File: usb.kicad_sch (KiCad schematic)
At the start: 17 parts, among them J2 USB_C_Receptacle, J3 Conn_01x02_Pin, Q1 STL6N3LLH6, U5 TCPP01-M12, U6 USBLC6-2P6, U7 STEF05SGR

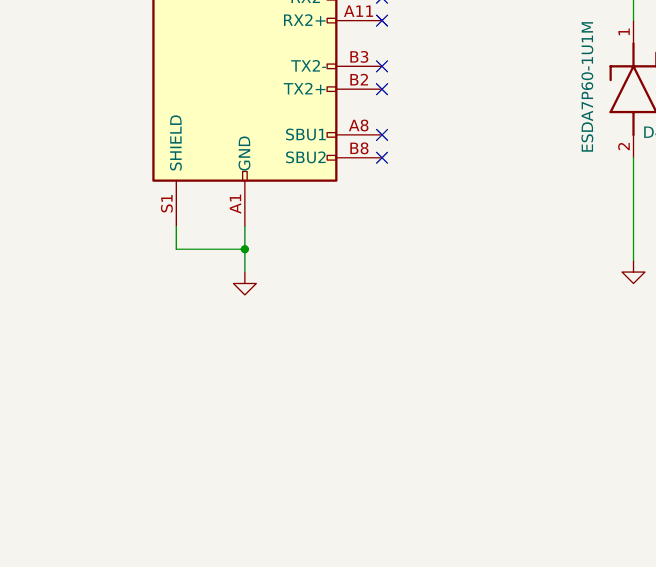
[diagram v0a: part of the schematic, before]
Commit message: only usb powered
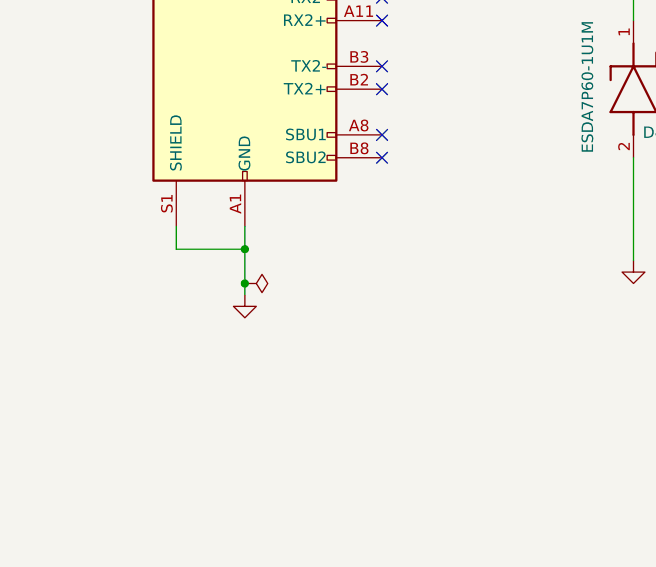
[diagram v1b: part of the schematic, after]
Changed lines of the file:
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@@
 	)
 	(junction
+		(at 33.02 132.08)
+		(diameter 0)
+		(color 0 0 0 0)
+	)
+	(junction
 		(at 267.97 110.49)
 		(diameter 0)
@@
 	(wire
 		(pts
+			(xy 33.02 132.08) (xy 33.02 133.35)
+		)
+		(stroke
+			(width 0)
+			(type default)
+		)
+	)
+	(wire
+		(pts
 			(xy 247.65 113.03) (xy 267.97 113.03)
 		)
@@
 	(wire
 		(pts
-			(xy 33.02 128.27) (xy 33.02 130.81)
+			(xy 33.02 128.27) (xy 33.02 132.08)
 		)
 		(stroke
@@
 			(project ""
 				(path "/e660428c-c9b7-476c-8ac8-2d419f233469/7dd15615-8075-471d-b8bf-599b8660331d"
-					(reference "R401")
+					(reference "R201")
 					(unit 1)
 				)
@@
 			(project ""
 				(path "/e660428c-c9b7-476c-8ac8-2d419f233469/7dd15615-8075-471d-b8bf-599b8660331d"
-					(reference "#PWR0409")
+					(reference "#PWR0209")
 					(unit 1)
 				)
@@
 	(symbol
 		(lib_id "power:GND")
-		(at 33.02 130.81 0)
+		(at 33.02 133.35 0)
 		(unit 1)
 		(exclude_from_sim no)
@@
 		(fields_autoplaced yes)
 		(property "Reference" "#PWR041"
-			(at 33.02 137.16 0)
+			(at 33.02 139.7 0)
 			(effects
 				(font
@@
 		)
 		(property "Value" "GND"
-			(at 33.02 135.89 0)
+			(at 33.02 138.43 0)
 			(effects
 				(font
@@
 		)
 		(property "Footprint" ""
-			(at 33.02 130.81 0)
+			(at 33.02 133.35 0)
 			(effects
 				(font
@@
 		)
 		(property "Datasheet" ""
-			(at 33.02 130.81 0)
+			(at 33.02 133.35 0)
 			(effects
 				(font
@@
 		)
 		(property "Description" "Power symbol creates a global label with name \"GND\" , ground"
-			(at 33.02 130.81 0)
+			(at 33.02 133.35 0)
 			(effects
 				(font
@@
 			(project ""
 				(path "/e660428c-c9b7-476c-8ac8-2d419f233469/7dd15615-8075-471d-b8bf-599b8660331d"
-					(reference "#PWR0413")
+					(reference "#PWR0214")
 					(unit 1)
 				)
@@
 			(project ""
 				(path "/e660428c-c9b7-476c-8ac8-2d419f233469/7dd15615-8075-471d-b8bf-599b8660331d"
-					(reference "#PWR0412")
+					(reference "#PWR0212")
 					(unit 1)
 				)
@@
 			(project ""
 				(path "/e660428c-c9b7-476c-8ac8-2d419f233469/7dd15615-8075-471d-b8bf-599b8660331d"
-					(reference "#PWR0411")
+					(reference "#PWR0211")
 					(unit 1)
 				)
@@
 			(project ""
 				(path "/e660428c-c9b7-476c-8ac8-2d419f233469/7dd15615-8075-471d-b8bf-599b8660331d"
-					(reference "#PWR0407")
+					(reference "#PWR0207")
 					(unit 1)
 				)
@@
 			(project ""
 				(path "/e660428c-c9b7-476c-8ac8-2d419f233469/7dd15615-8075-471d-b8bf-599b8660331d"
-					(reference "D402")
+					(reference "D202")
 					(unit 1)
 				)
@@
 			(project ""
 				(path "/e660428c-c9b7-476c-8ac8-2d419f233469/7dd15615-8075-471d-b8bf-599b8660331d"
-					(reference "#PWR0419")
+					(reference "#PWR0219")
 					(unit 1)
 				)
@@
 			(project ""
 				(path "/e660428c-c9b7-476c-8ac8-2d419f233469/7dd15615-8075-471d-b8bf-599b8660331d"
-					(reference "D401")
+					(reference "D201")
 					(unit 1)
 				)
@@
 			(project ""
 				(path "/e660428c-c9b7-476c-8ac8-2d419f233469/7dd15615-8075-471d-b8bf-599b8660331d"
-					(reference "#PWR0408")
+					(reference "#PWR0208")
 					(unit 1)
 				)
@@
 			(project ""
 				(path "/e660428c-c9b7-476c-8ac8-2d419f233469/7dd15615-8075-471d-b8bf-599b8660331d"
-					(reference "#PWR0418")
+					(reference "#PWR0218")
 					(unit 1)
 				)
@@
 			(project ""
 				(path "/e660428c-c9b7-476c-8ac8-2d419f233469/7dd15615-8075-471d-b8bf-599b8660331d"
-					(reference "#FLG0403")
+					(reference "#FLG0203")
 					(unit 1)
 				)
@@
 			(project ""
 				(path "/e660428c-c9b7-476c-8ac8-2d419f233469/7dd15615-8075-471d-b8bf-599b8660331d"
-					(reference "#PWR0406")
+					(reference "#PWR0206")
 					(unit 1)
 				)
@@
 			(project ""
 				(path "/e660428c-c9b7-476c-8ac8-2d419f233469/7dd15615-8075-471d-b8bf-599b8660331d"
-					(reference "#PWR0410")
+					(reference "#PWR0210")
 					(unit 1)
 				)
@@
 			(project ""
 				(path "/e660428c-c9b7-476c-8ac8-2d419f233469/7dd15615-8075-471d-b8bf-599b8660331d"
-					(reference "#PWR0401")
+					(reference "#PWR0201")
 					(unit 1)
 				)
@@
 			(project ""
 				(path "/e660428c-c9b7-476c-8ac8-2d419f233469/7dd15615-8075-471d-b8bf-599b8660331d"
-					(reference "J402")
+					(reference "J202")
 					(unit 1)
 				)
@@
 			(project ""
 				(path "/e660428c-c9b7-476c-8ac8-2d419f233469/7dd15615-8075-471d-b8bf-599b8660331d"
-					(reference "Q401")
+					(reference "Q201")
 					(unit 1)
 				)
@@
 			(project ""
 				(path "/e660428c-c9b7-476c-8ac8-2d419f233469/7dd15615-8075-471d-b8bf-599b8660331d"
-					(reference "U401")
+					(reference "U201")
 					(unit 1)
 				)
@@
 			(project ""
 				(path "/e660428c-c9b7-476c-8ac8-2d419f233469/7dd15615-8075-471d-b8bf-599b8660331d"
-					(reference "#FLG0402")
+					(reference "#FLG0202")
 					(unit 1)
 				)
@@
 			(project ""
 				(path "/e660428c-c9b7-476c-8ac8-2d419f233469/7dd15615-8075-471d-b8bf-599b8660331d"
-					(reference "TP402")
+					(reference "TP202")
+					(unit 1)
+				)
+			)
+		)
+	)
+	(symbol
+		(lib_id "power:PWR_FLAG")
+		(at 33.02 132.08 270)
+		(unit 1)
+		(exclude_from_sim no)
+		(in_bom yes)
+		(on_board yes)
+		(dnp no)
+		(fields_autoplaced yes)
+		(property "Reference" "#FLG0204"
+			(at 34.925 132.08 0)
+			(effects
+				(font
+					(size 1.27 1.27)
+				)
+				(hide yes)
+			)
+		)
+		(property "Value" "PWR_FLAG"
+			(at 36.83 132.0801 90)
+			(effects
+				(font
+					(size 1.27 1.27)
+				)
+				(justify left)
+				(hide yes)
+			)
+		)
+		(property "Footprint" ""
+			(at 33.02 132.08 0)
+			(effects
+				(font
+					(size 1.27 1.27)
+				)
+				(hide yes)
+			)
+		)
+		(property "Datasheet" "~"
+			(at 33.02 132.08 0)
+			(effects
+				(font
+					(size 1.27 1.27)
+				)
+				(hide yes)
+			)
+		)
+		(property "Description" "Special symbol for telling ERC where power comes from"
+			(at 33.02 132.08 0)
+			(effects
+				(font
+					(size 1.27 1.27)
+				)
+				(hide yes)
+			)
+		)
+		(pin "1"
+		)
+		(instances
+			(project "EnergyMonitoringSystem"
+				(path "/e660428c-c9b7-476c-8ac8-2d419f233469/7dd15615-8075-471d-b8bf-599b8660331d"
+					(reference "#FLG0204")
 					(unit 1)
 				)
@@
 			(project ""
 				(path "/e660428c-c9b7-476c-8ac8-2d419f233469/7dd15615-8075-471d-b8bf-599b8660331d"
-					(reference "J401")
+					(reference "J201")
 					(unit 1)
 				)
@@
 			(project ""
 				(path "/e660428c-c9b7-476c-8ac8-2d419f233469/7dd15615-8075-471d-b8bf-599b8660331d"
-					(reference "#PWR0416")
+					(reference "#PWR0216")
 					(unit 1)
 				)
@@
 			(project ""
 				(path "/e660428c-c9b7-476c-8ac8-2d419f233469/7dd15615-8075-471d-b8bf-599b8660331d"
-					(reference "R402")
+					(reference "R202")
 					(unit 1)
 				)
@@
 			(project ""
 				(path "/e660428c-c9b7-476c-8ac8-2d419f233469/7dd15615-8075-471d-b8bf-599b8660331d"
-					(reference "C404")
+					(reference "C204")
 					(unit 1)
 				)
@@
 			(project ""
 				(path "/e660428c-c9b7-476c-8ac8-2d419f233469/7dd15615-8075-471d-b8bf-599b8660331d"
-					(reference "TP401")
+					(reference "TP201")
 					(unit 1)
 				)
@@
 			(project ""
 				(path "/e660428c-c9b7-476c-8ac8-2d419f233469/7dd15615-8075-471d-b8bf-599b8660331d"
-					(reference "U402")
+					(reference "U202")
 					(unit 1)
 				)
@@
 			(project ""
 				(path "/e660428c-c9b7-476c-8ac8-2d419f233469/7dd15615-8075-471d-b8bf-599b8660331d"
-					(reference "#PWR0404")
+					(reference "#PWR0204")
 					(unit 1)
 				)
@@
 			(project ""
 				(path "/e660428c-c9b7-476c-8ac8-2d419f233469/7dd15615-8075-471d-b8bf-599b8660331d"
-					(reference "U403")
+					(reference "U203")
 					(unit 1)
 				)
@@
 			(project ""
 				(path "/e660428c-c9b7-476c-8ac8-2d419f233469/7dd15615-8075-471d-b8bf-599b8660331d"
-					(reference "#PWR0417")
+					(reference "#PWR0217")
 					(unit 1)
 				)
@@
 			(project ""
 				(path "/e660428c-c9b7-476c-8ac8-2d419f233469/7dd15615-8075-471d-b8bf-599b8660331d"
-					(reference "#PWR0402")
+					(reference "#PWR0202")
 					(unit 1)
 				)
@@
 			(project ""
 				(path "/e660428c-c9b7-476c-8ac8-2d419f233469/7dd15615-8075-471d-b8bf-599b8660331d"
-					(reference "#PWR0405")
+					(reference "#PWR0205")
 					(unit 1)
 				)
@@
 			(project ""
 				(path "/e660428c-c9b7-476c-8ac8-2d419f233469/7dd15615-8075-471d-b8bf-599b8660331d"
-					(reference "#PWR0415")
+					(reference "#PWR0215")
 					(unit 1)
 				)
@@
 			(project ""
 				(path "/e660428c-c9b7-476c-8ac8-2d419f233469/7dd15615-8075-471d-b8bf-599b8660331d"
-					(reference "R403")
+					(reference "R203")
 					(unit 1)
 				)
@@
 			(project ""
 				(path "/e660428c-c9b7-476c-8ac8-2d419f233469/7dd15615-8075-471d-b8bf-599b8660331d"
-					(reference "C401")
+					(reference "C201")
 					(unit 1)
 				)
@@
 			(project ""
 				(path "/e660428c-c9b7-476c-8ac8-2d419f233469/7dd15615-8075-471d-b8bf-599b8660331d"
-					(reference "C403")
+					(reference "C203")
 					(unit 1)
 				)
@@
 			(project ""
 				(path "/e660428c-c9b7-476c-8ac8-2d419f233469/7dd15615-8075-471d-b8bf-599b8660331d"
-					(reference "#PWR0403")
+					(reference "#PWR0203")
 					(unit 1)
 				)
@@
 			(project ""
 				(path "/e660428c-c9b7-476c-8ac8-2d419f233469/7dd15615-8075-471d-b8bf-599b8660331d"
-					(reference "C402")
+					(reference "C202")
 					(unit 1)
 				)
@@
 			(project ""
 				(path "/e660428c-c9b7-476c-8ac8-2d419f233469/7dd15615-8075-471d-b8bf-599b8660331d"
-					(reference "#PWR0414")
+					(reference "#PWR0213")
 					(unit 1)
 				)
@@
 			(project ""
 				(path "/e660428c-c9b7-476c-8ac8-2d419f233469/7dd15615-8075-471d-b8bf-599b8660331d"
-					(reference "#FLG0401")
+					(reference "#FLG0201")
 					(unit 1)
 				)

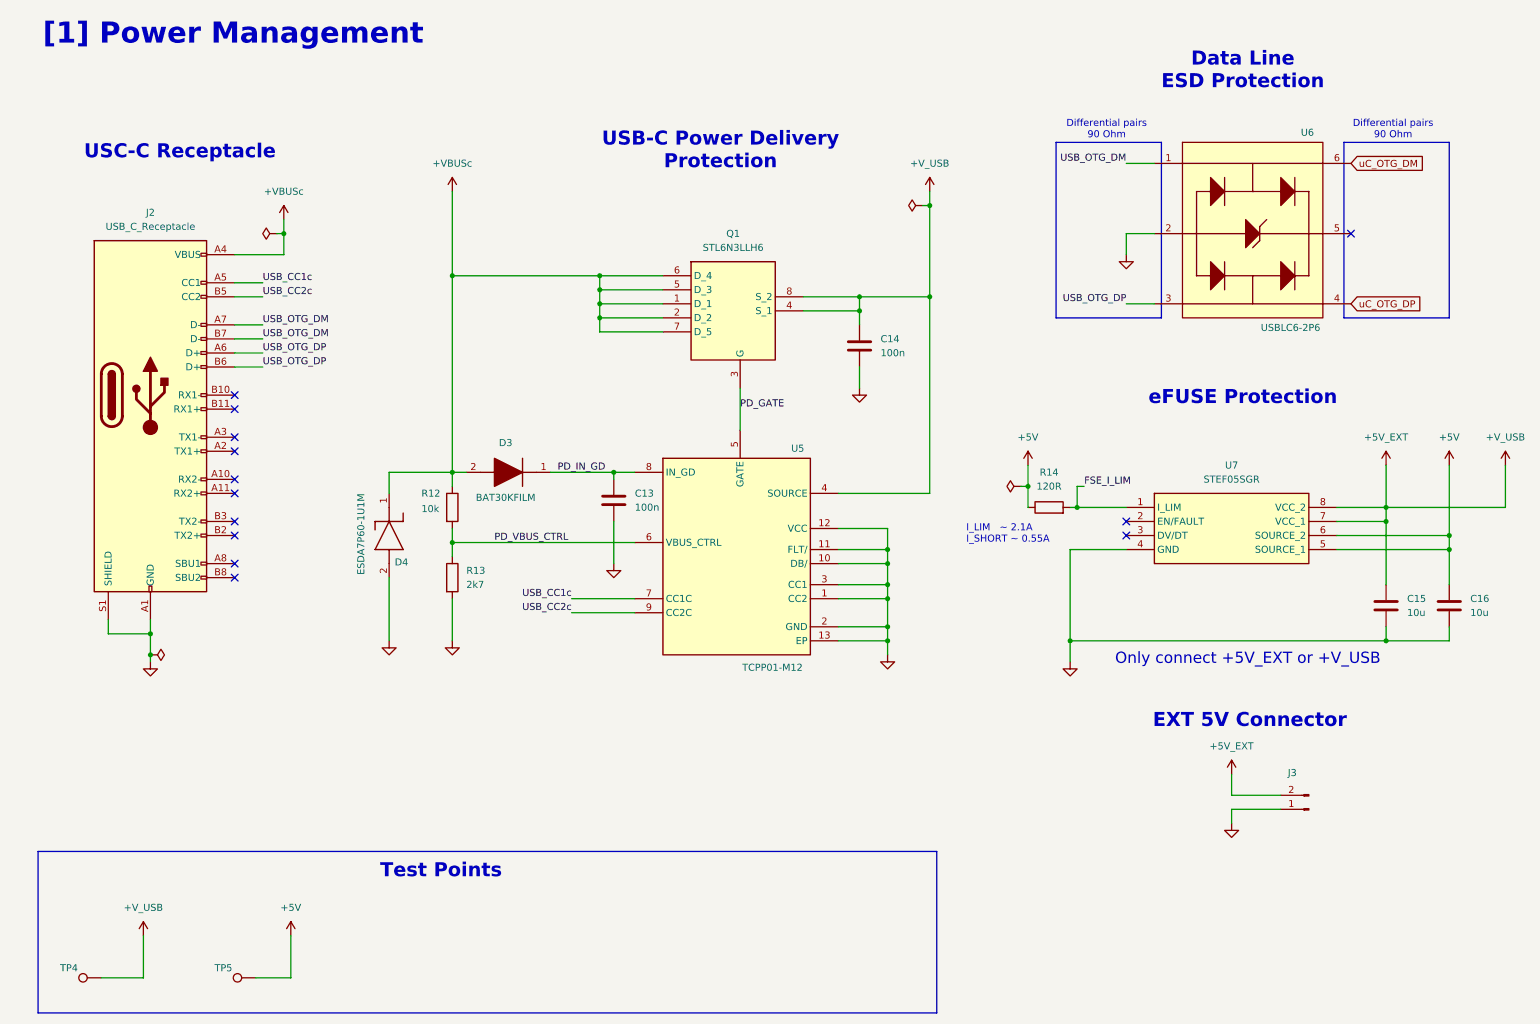
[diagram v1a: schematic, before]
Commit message: components with distributor links added
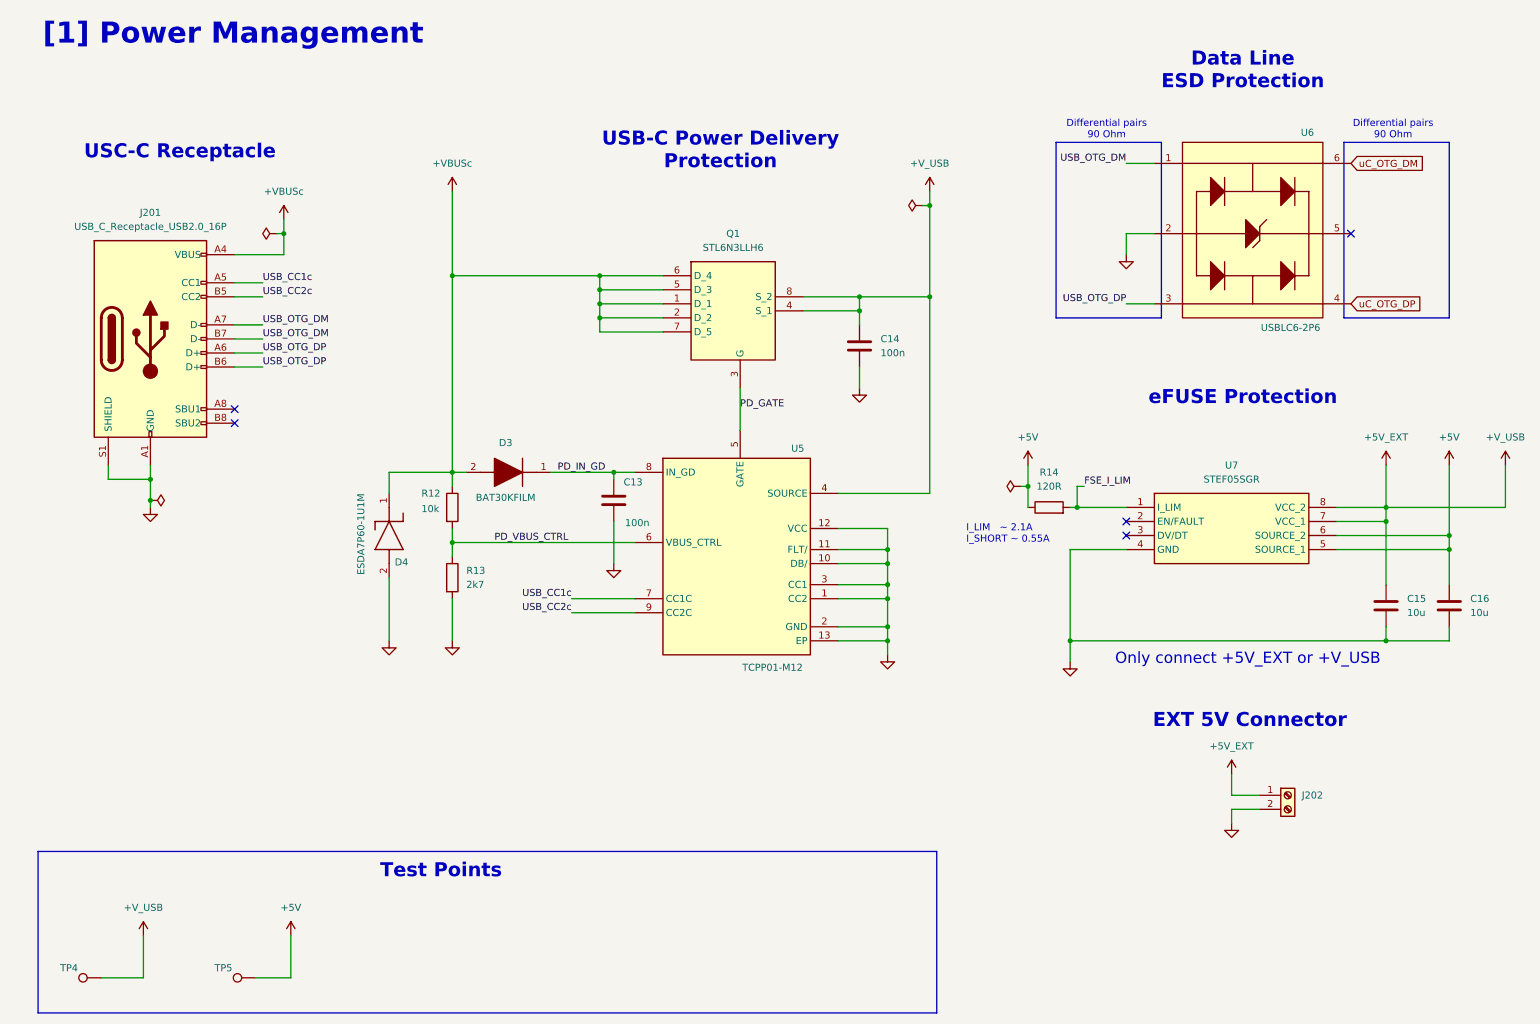
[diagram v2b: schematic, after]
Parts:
- removed J2: USB_C_Receptacle, Connector_USB:USB_C_Receptacle_GCT_USB4105-xx-A_16P_TopMnt_Horizontal, symbol Connector:USB_C_Receptacle
- removed J3: Conn_01x02_Pin, TerminalBlock_Phoenix:TerminalBlock_Phoenix_MKDS-1,5-2-5.08_1x02_P5.08mm_Horizontal, symbol Connector:Conn_01x02_Pin
- added J201: USB_C_Receptacle_USB2.0_16P, Connector_USB:USB_C_Receptacle_GCT_USB4105-xx-A_16P_TopMnt_Horizontal, symbol Connector:USB_C_Receptacle_USB2.0_16P
- added J202: Screw_Terminal_01x02, TerminalBlock_Phoenix:TerminalBlock_Phoenix_MKDS-1,5-2-5.08_1x02_P5.08mm_Horizontal, symbol Connector:Screw_Terminal_01x02
- C13, C14: Distributor_Link (none) -> https://www.mouser.com/ProductDetail/KYOCERA-AVX/04023C104K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; Manufacturer_Name (none) -> KYOCERA AVX; Manufacturer_Part_Number (none) -> 04023C104KAT2A
- C15, C16: Distributor_Link (none) -> https://www.mouser.com/ProductDetail/KYOCERA-AVX/KGM15CR51A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; Manufacturer_Name (none) -> KYOCERA AVX; Manufacturer_Part_Number (none) -> KGM15CR51A106KT
- D3: Distributor_Link (none) -> https://www.mouser.co.uk/ProductDetail/STMicroelectronics/B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
- D4: Distributor_Link (none) -> https://www.mouser.co.uk/ProductDetail/STMicroelectronics/E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
- Q1, U7: Distributor_Link (none) -> https://www.mouser.co.uk/ProductDetail/STMicroelectronics/S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
- R12: Distributor_Link (none) -> https://www.mouser.com/ProductDetail/Vishay-Dale/CRCW060310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; Manufacturer_Name (none) -> Vishay/Dale; Manufacturer_Part_Number (none) -> CRCW060310K0FKEI
- R13: Distributor_Link (none) -> https://www.mouser.com/ProductDetail/ROHM-Semiconductor/SFR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; Manufacturer_Name (none) -> ROHM Semiconductor; Manufacturer_Part_Number (none) -> SFR03EZPF2701
- R14: footprint Resistor_SMD:R_0603_1608Metric -> Resistor_SMD:R_0402_1005Metric; Distributor_Link (none) -> https://www.mouser.com/ProductDetail/ROHM-Semiconductor/SFR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; Manufacturer_Name (none) -> ROHM Semiconductor; Manufacturer_Part_Number (none) -> SFR01MZPF1200
- TP4, TP5: footprint TestPoint:TestPoint_Loop_D3.50mm_Drill1.4mm_Beaded -> EMS:5000; Distributor_Link (none) -> https://www.mouser.com/ProductDetail/Keystone-Electronics/5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; Manufacturer_Name (none) -> Keystone Electronics; Manufacturer_Part_Number (none) -> 5000
- U5: Distributor_Link (none) -> https://www.mouser.co.uk/ProductDetail/STMicroelectronics/T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
- U6: Distributor_Link (none) -> https://www.mouser.co.uk/ProductDetail/STMicroelectronics/U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
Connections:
- net +5V_EXT: now also J202.1 (Pin_1)
- net +VBUSc: now also J201.A4 (VBUS), J201.A9 (VBUS), J201.B4 (VBUS), J201.B9 (VBUS)
- net GND: now also J201.A1 (GND), J201.A12 (GND), J201.B1 (GND), J201.B12 (GND), J201.S1 (SHIELD), J202.2 (Pin_2)
- net USB_CC1c: now also J201.A5 (CC1)
- net USB_CC2c: now also J201.B5 (CC2)
- net USB_OTG_DM: now also J201.A7 (D-), J201.B7 (D-)
- net USB_OTG_DP: now also J201.A6 (D+), J201.B6 (D+)
- no-connect marks 13 -> 5
